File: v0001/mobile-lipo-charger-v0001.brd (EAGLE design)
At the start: 83 x 93.5 mm, 48 parts, among them IC1 AD8610MR, IC2 STM32F401VBT, IC3 AD8610MR, SW1 DHT-4235A, U3 3.3V

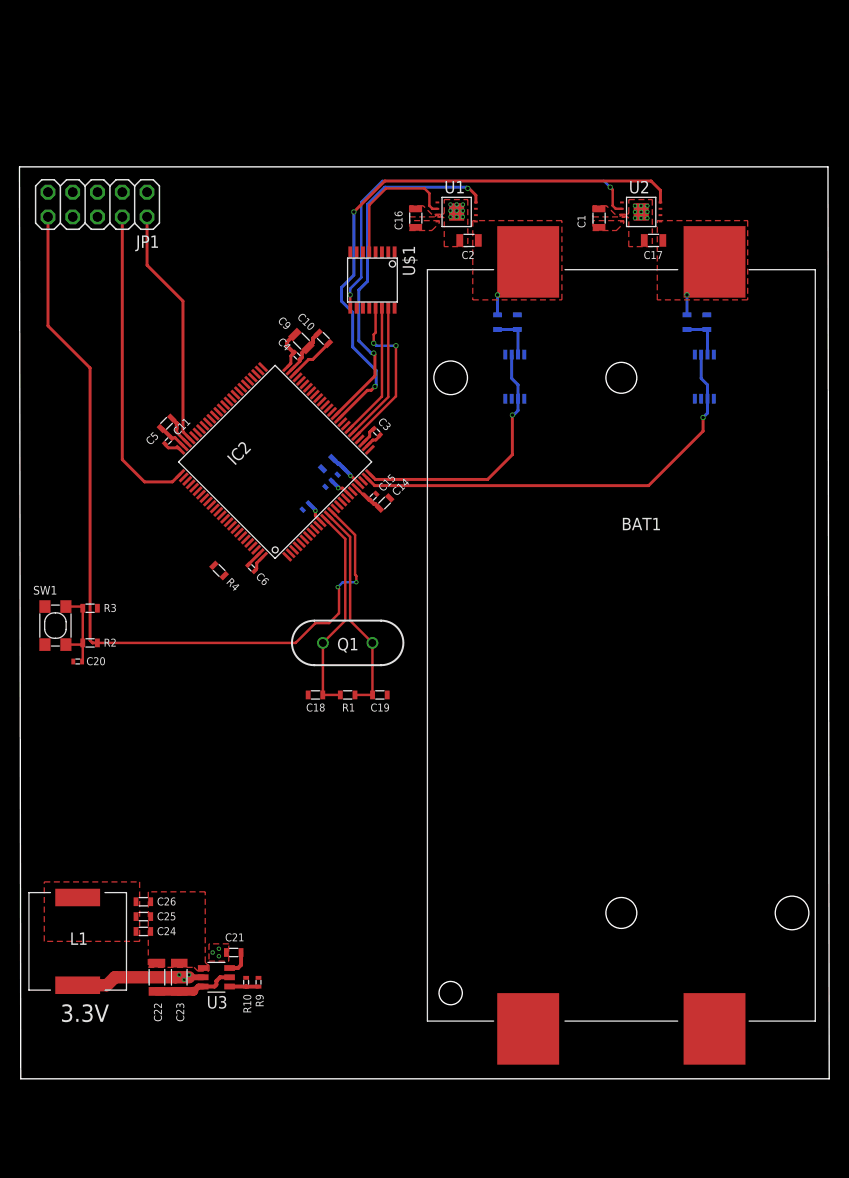
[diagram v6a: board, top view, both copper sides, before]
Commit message: Minor Changes
Made minor changes to the polygons for the charger chips
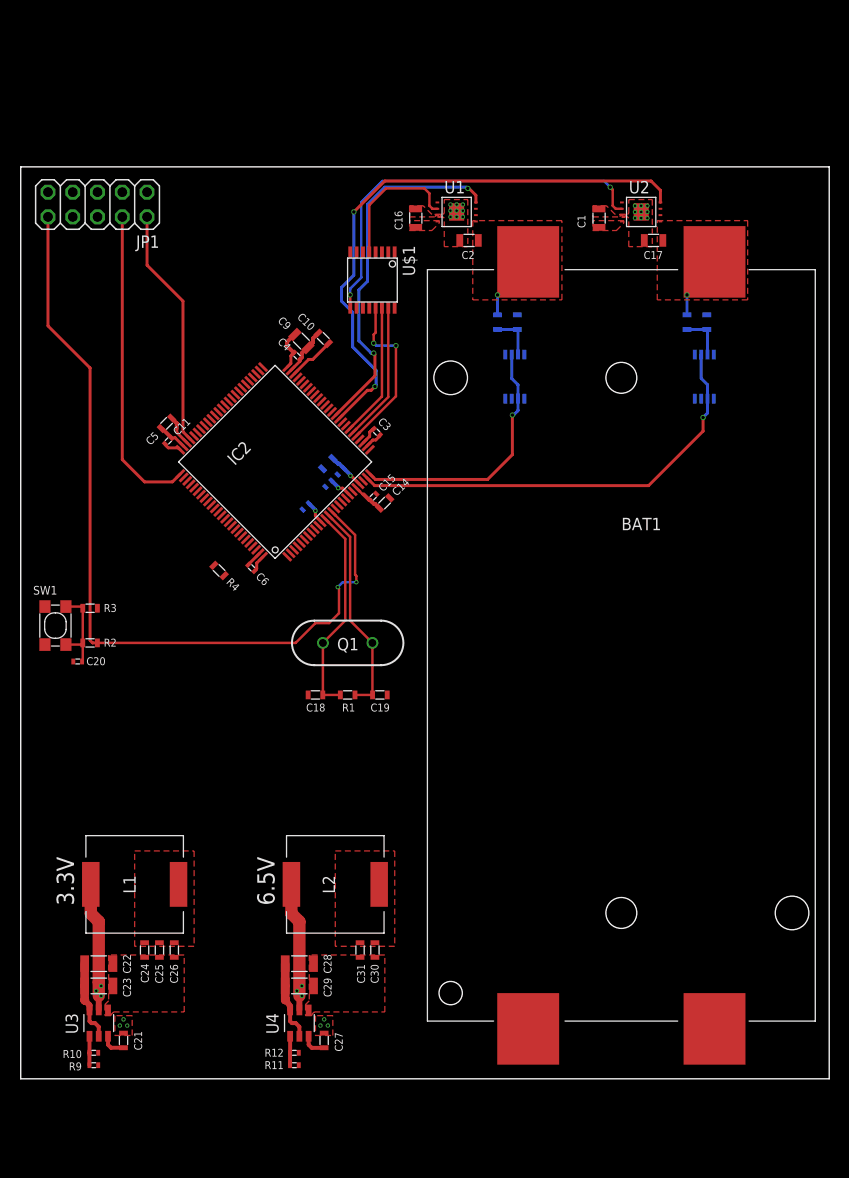
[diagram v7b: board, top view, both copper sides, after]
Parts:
- added C27: 100n, common:0603L3
- added C28, C29: 10u, common:1206L3
- added C30, C31: 22u, common:0603L3
- added L2: 3.3uH, common:10X10
- added R11: 75k, common:0402L3
- added R12: 10k, common:0402L3
- added U4: 3.3V, common:SOT-1.1
- moved R9 18.9 mm to (7.49, 12.3), turned to 0 degrees
- moved R10 17.2 mm to (7.49, 13.6), turned to 180 degrees
- moved C21 14.5 mm to (10.5, 14.9), turned to 270 degrees
- moved U3 12.9 mm to (8.00, 16.6), turned to 270 degrees
- moved C23 8.30 mm to (8.00, 20.4), turned to 0 degrees
- moved L1 8.26 mm to (11.7, 30.9), turned to 270 degrees
- moved C22 6.13 mm to (8.00, 22.7), turned to 0 degrees
- moved C26 5.88 mm to (15.7, 24.1), turned to 270 degrees
- moved C25 3.81 mm to (14.2, 24.1), turned to 270 degrees
- moved C24 1.91 mm to (12.7, 24.1), turned to 270 degrees
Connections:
- new net SW2: C27.P$1, L2.1, U4.2
- new net VBST2: C27.P$2, U4.6
- new net VFB2: R11.P$1, R12.P$2, U4.4
- new net VIN_CHARGER: C1.1, C16.1, C30.P$1, C31.P$1, L2.2, R11.P$2, U1.4, U2.4
- net BATT+: now also C28.1, C29.1, U4.3, U4.5; no longer C1.1, C16.1, U1.4, U2.4
- net GND: now also C28.2, C29.2, C30.P$2, C31.P$2, R12.P$1, U4.1
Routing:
- net SW2: track 0.00 -> 14.8 mm, vias 0 -> 6
- net BATT+: track 8.27 -> 16.6 mm
- net VFB2: track 0.00 -> 2.97 mm
- net VBST2: track 0.00 -> 2.60 mm
- added copper zone on layer 1, net SW2
- added copper zone on layer 2, net SW2
- added copper zone on layer 1, net VIN_CHARGER
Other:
- board size 83 x 93.5 mm -> 82.9 x 93.5 mm
- board text added: "6.5V"
